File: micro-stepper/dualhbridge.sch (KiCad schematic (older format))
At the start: 10 parts, among them U201 4011, U202 4081, U203 MOSPAIR, U204 MOSPAIR, U205 MOSPAIR, U206 MOSPAIR

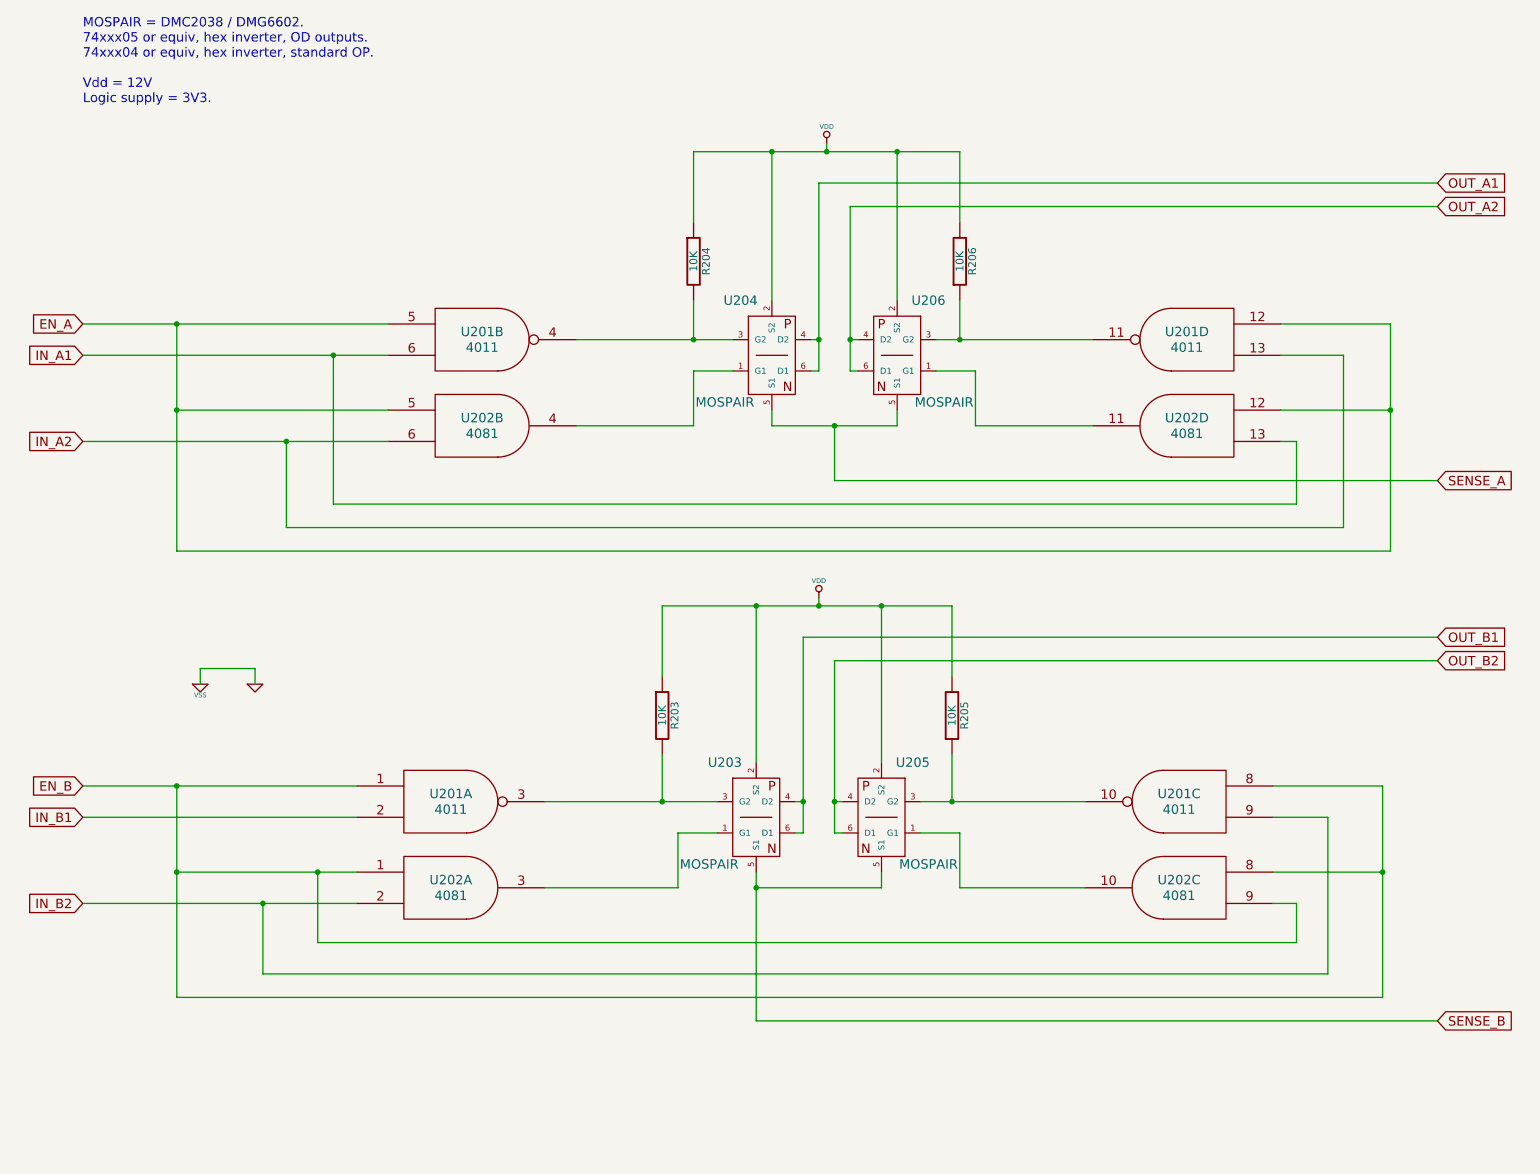
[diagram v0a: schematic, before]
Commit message: Update schematic, PCB
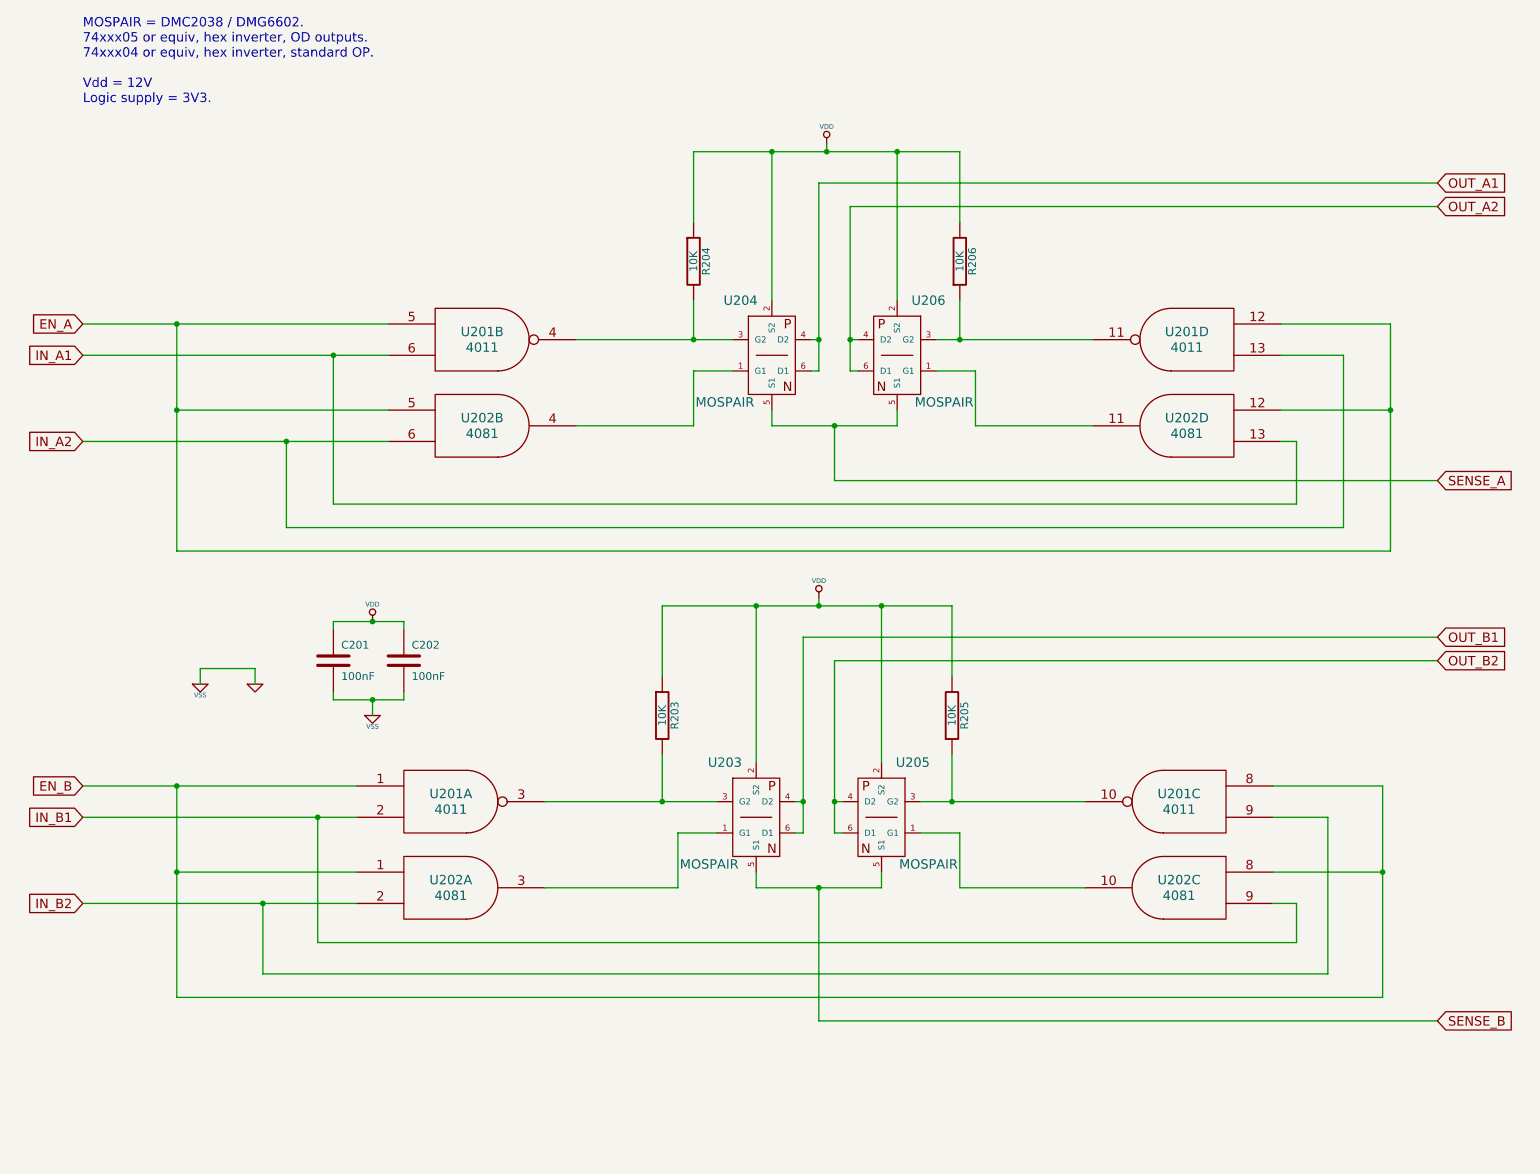
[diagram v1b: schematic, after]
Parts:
- added C201, C202: 100nF, symbol C
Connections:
- net EN_B: no longer U202.9
- net GND: now also C201.2, C202.2
- net IN_B1: now also U202.9
- net VDD: now also C201.1, C202.1

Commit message: Update gate drive on P-FETS; remove external diodes
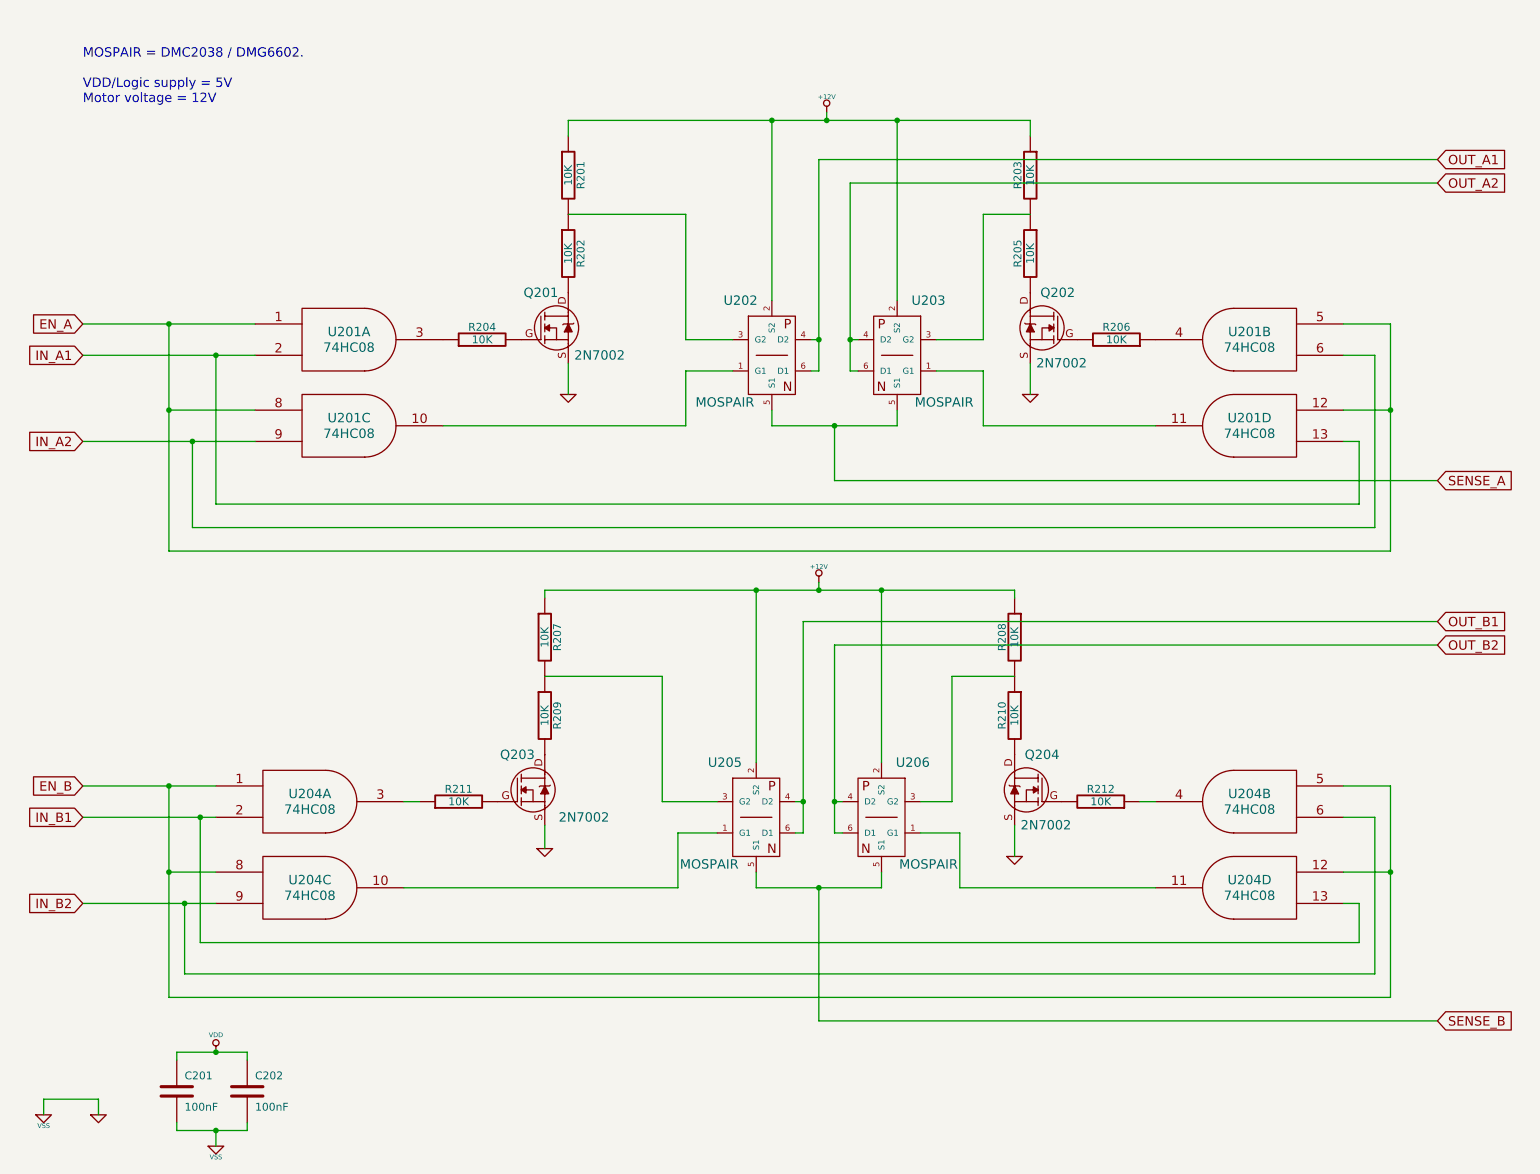
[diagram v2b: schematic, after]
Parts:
- removed U201: 4011, symbol 4011
- added Q201, Q202, Q203, Q204: 2N7002, symbol MOSFET_N_RMC
- added R201, R204, R207, R208, R209, R210, R211, R212: 10K, symbol R
- added unit 1 of U201
- added unit 2 of U201
- added unit 2 of U204
- added unit 1 of U204
- U201, U204: renamed from U202; value 4081 -> 74HC08
- renumbered R204 to R202, U204 to U202, U206 to U203, U203 to U205, U205 to U206
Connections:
- net EN_A: now also U201.8, U201.1, U201.5; no longer U201.5
- net EN_B: now also U204.12, U204.8, U204.1, U204.5; no longer U204.1, U204.8
- net GND: now also Q201.S, Q202.S, Q203.S, Q204.S, U201.7 (VSS), U201.7 (VSS), U204.7 (VSS), U204.7 (VSS)
- net IN_A1: now also U201.2
- net IN_A2: now also U201.9, U201.6; no longer U201.6
- net IN_B1: now also U204.13, U204.2; no longer U204.9
- net IN_B2: now also U204.9, U204.6; no longer U204.2
- net VDD: now also U201.14 (VDD), U201.14 (VDD), U204.14 (VDD), U204.14 (VDD); no longer R202.1, R203.1, R205.2, R206.2, U202.2 (S2), U203.2 (S2), U205.2 (S2), U206.2 (S2)
- net at U206.1 (G1): now also U204.11; no longer U204.10
- net at U206.3 (G2): now also R208.2, R210.1; no longer R205.1
- net at U203.3 (G2): now also R203.2, R205.1; no longer R206.1
- net at U205.3 (G2): now also R207.2, R209.1; no longer R203.2
- net at U202.3 (G2): now also R202.1, R201.2; no longer R202.2
- net at U205.1 (G1): now also U204.10; no longer U204.3
- net at U202.1 (G1): now also U201.10; no longer U201.4
- new net: Q201.D, R202.2
- new net: Q201.G, R204.2
- new net: R204.1, U201.3
- new net: R206.1, U201.4
- new net: R212.1, U204.4
- new net: R211.1, U204.3
- new net: Q202.G, R206.2
- new net: Q202.D, R205.2
- new net: Q203.G, R211.2
- new net: Q203.D, R209.2
- new net: Q204.D, R210.2
- new net: Q204.G, R212.2
- new net +12V: R201.1, R203.1, R207.1, R208.1, U202.2 (S2), U203.2 (S2), U205.2 (S2), U206.2 (S2)
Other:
- note added: "MOSPAIR = DMC2038 / DMG6602.\n\nVDD/Logic supply = 5V\nMotor voltage = 12V\n"
- note removed: "MOSPAIR = DMC2038 / DMG6602.\n74xxx05 or equiv, hex inverter, OD outputs.\n74xxx04 or equiv, hex inverter, standard OP.\n\nVdd = 12V\nLogic supply = 3V3."
- moved on the sheet: C201, C202, R202, U201D
